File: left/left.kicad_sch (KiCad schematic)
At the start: 4 parts, among them J1 HDMI_C_1.4, SW1 SW_Push_Dual, U1 Raspberry_Pi_Pico

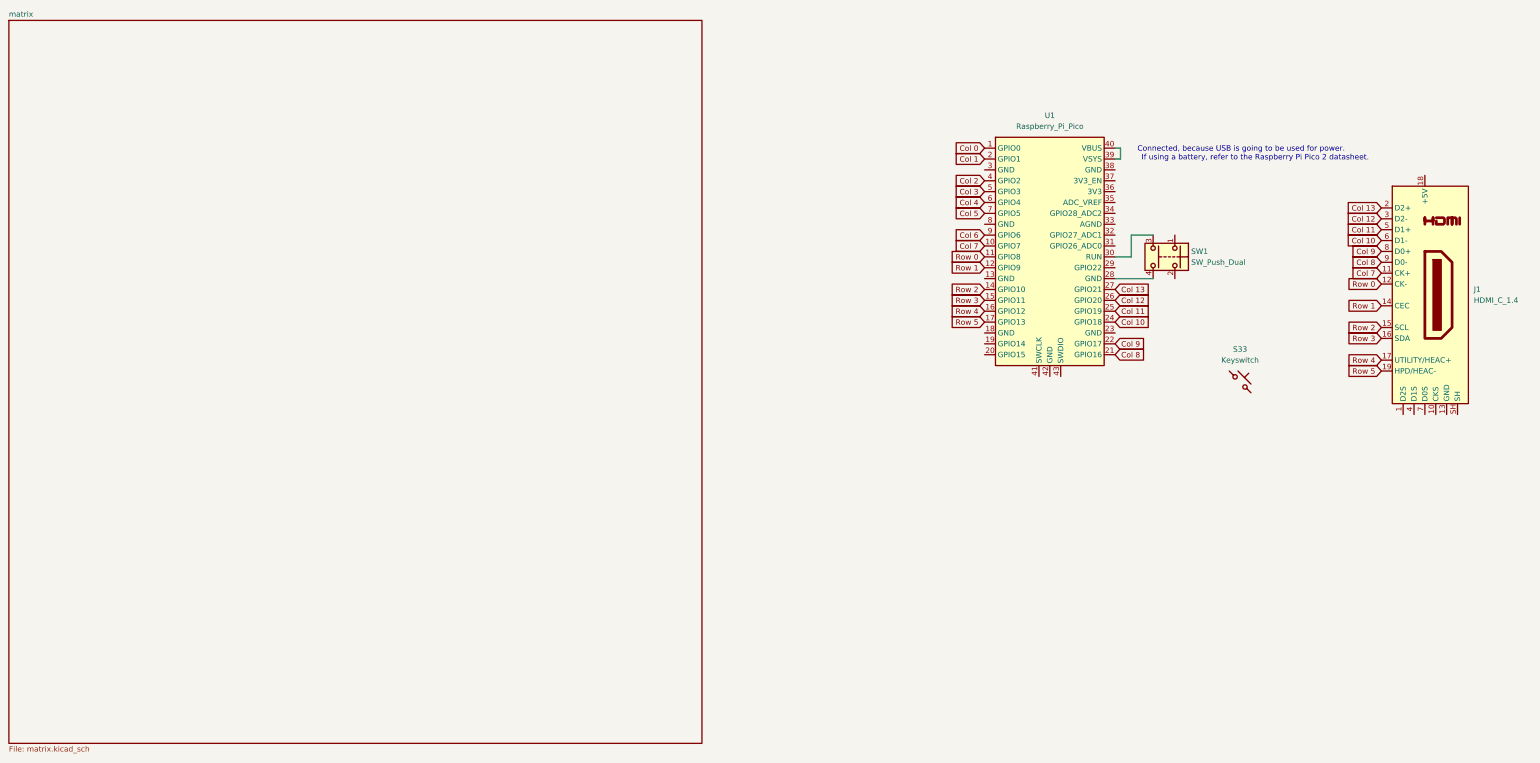
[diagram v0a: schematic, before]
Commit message: Fix issues from update to KiCad 9
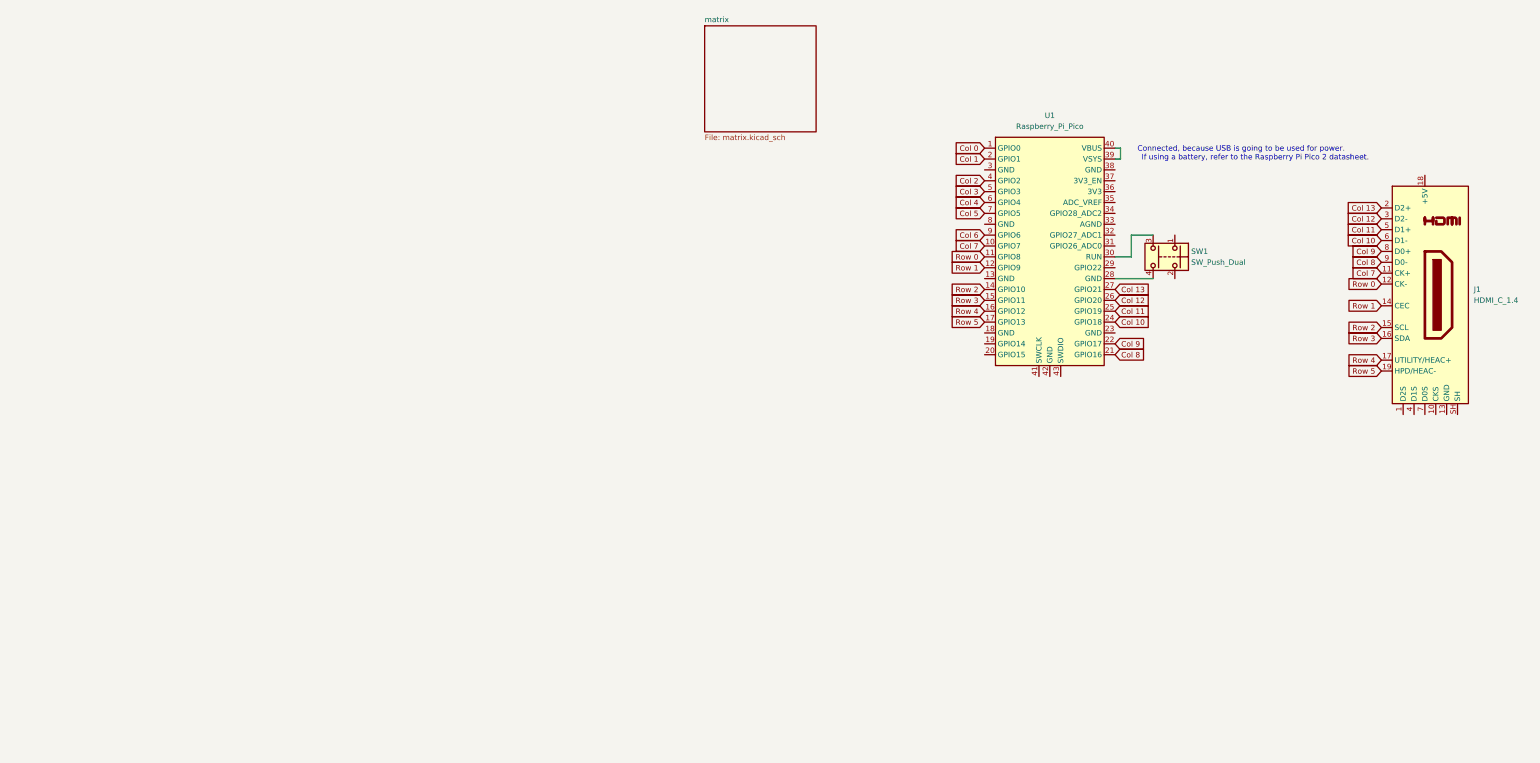
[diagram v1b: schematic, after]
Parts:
- removed S33: Keyswitch, ScottoKeebs_Hotswap:Hotswap_MX_1.00u, symbol ScottoKeebs:Placeholder_Keyswitch
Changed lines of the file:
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@@
 (kicad_sch
-	(version 20231120)
+	(version 20250114)
 	(generator "eeschema")
-	(generator_version "8.0")
+	(generator_version "9.0")
 	(paper "A4")
+	(text "If using a battery, refer to the Raspberry Pi Pico 2 datasheet.\n"
+		(exclude_from_sim no)
+		(at 96.266 31.496 0)
+		(effects
+			(font
+				(size 1.27 1.27)
+			)
+		)
+	)
+	(text "Connected, because USB is going to be used for power."
+		(exclude_from_sim no)
+		(at 92.964 29.464 0)
+		(effects
+			(font
+				(size 1.27 1.27)
+			)
+		)
+	)
 	(wire
 		(pts
@@
 		)
 	)
-	(text "If using a battery, refer to the Raspberry Pi Pico 2 datasheet.\n"
-		(exclude_from_sim no)
-		(at 96.266 31.496 0)
-		(effects
-			(font
-				(size 1.27 1.27)
-			)
-		)
-	)
-	(text "Connected, because USB is going to be used for power."
-		(exclude_from_sim no)
-		(at 92.964 29.464 0)
-		(effects
-			(font
-				(size 1.27 1.27)
-			)
-		)
-	)
 	(global_label "Row 2"
 		(shape input)
@@
 				(justify right)
 				(hide yes)
-			)
-		)
-	)
-	(symbol
-		(lib_id "ScottoKeebs:Placeholder_Keyswitch")
-		(at 92.71 83.82 0)
-		(unit 1)
-		(exclude_from_sim no)
-		(in_bom yes)
-		(on_board yes)
-		(dnp no)
-		(fields_autoplaced yes)
-		(property "Reference" "S33"
-			(at 92.71 76.2 0)
-			(effects
-				(font
-					(size 1.27 1.27)
-				)
-			)
-		)
-		(property "Value" "Keyswitch"
-			(at 92.71 78.74 0)
-			(effects
-				(font
-					(size 1.27 1.27)
-				)
-			)
-		)
-		(property "Footprint" "ScottoKeebs_Hotswap:Hotswap_MX_1.00u"
-			(at 92.71 83.82 0)
-			(effects
-				(font
-					(size 1.27 1.27)
-				)
-				(hide yes)
-			)
-		)
-		(property "Datasheet" "~"
-			(at 92.71 83.82 0)
-			(effects
-				(font
-					(size 1.27 1.27)
-				)
-				(hide yes)
-			)
-		)
-		(property "Description" "Push button switch, normally open, two pins, 45° tilted"
-			(at 92.71 83.82 0)
-			(effects
-				(font
-					(size 1.27 1.27)
-				)
-				(hide yes)
-			)
-		)
-		(pin "2"
-		)
-		(pin "1"
-		)
-		(instances
-			(project ""
-				(path "/6768e4e1-ee9a-4437-ba1f-295b12420b2f"
-					(reference "S33")
-					(unit 1)
-				)
 			)
 		)
@@
 	)
 	(sheet
-		(at -194.945 -0.635)
-		(size 161.925 168.91)
+		(at -32.385 0.635)
+		(size 26.035 24.765)
+		(exclude_from_sim no)
+		(in_bom yes)
+		(on_board yes)
+		(dnp no)
 		(fields_autoplaced yes)
 		(stroke
@@
 		)
 		(property "Sheetname" "matrix"
-			(at -194.945 -1.3466 0)
+			(at -32.385 -0.0766 0)
 			(effects
 				(font
@@
 		)
 		(property "Sheetfile" "matrix.kicad_sch"
-			(at -194.945 168.8596 0)
+			(at -32.385 25.9846 0)
 			(effects
 				(font
@@
 		)
 	)
+	(embedded_fonts no)
 )

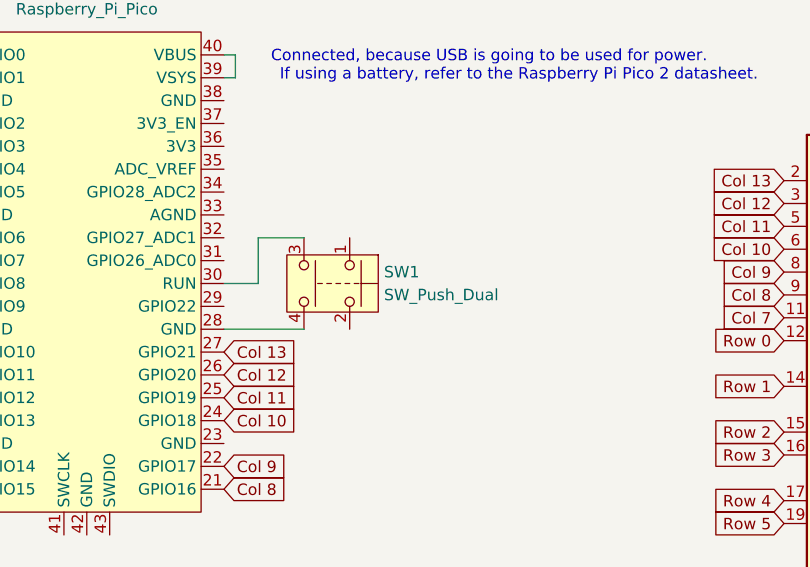
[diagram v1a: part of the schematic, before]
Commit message: Add OSHW logo
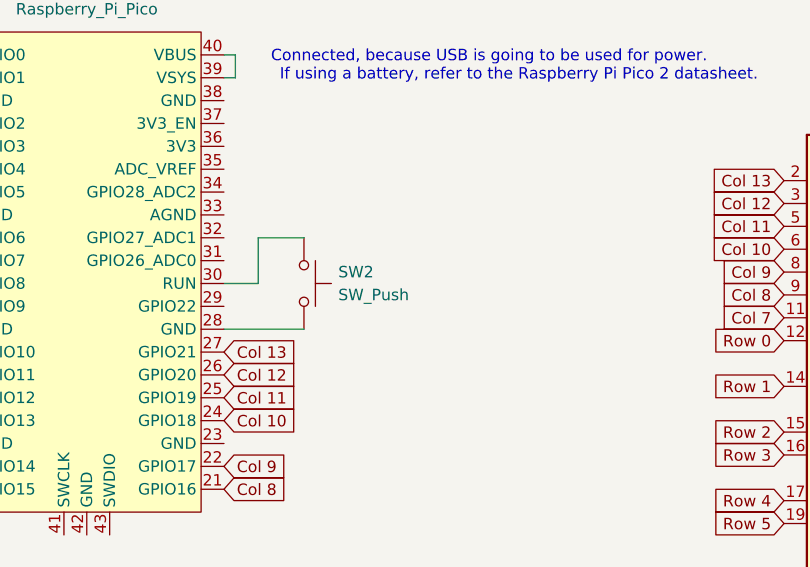
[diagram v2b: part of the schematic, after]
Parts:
- removed SW1: SW_Push_Dual, symbol Switch:SW_Push_Dual
- added SW2: SW_Push, Button_Switch_SMD:Panasonic_EVQPUJ_EVQPUA, symbol Switch:SW_Push
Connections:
- net at U1.30 (RUN): now also SW2.1
- net at U1.28 (GND): now also SW2.2
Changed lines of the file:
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@@
-	)
-	(symbol
-		(lib_id "Switch:SW_Push_Dual")
-		(at 74.93 54.61 270)
-		(unit 1)
-		(exclude_from_sim no)
-		(in_bom yes)
-		(on_board yes)
-		(dnp no)
-		(fields_autoplaced yes)
-		(property "Reference" "SW1"
-			(at 81.28 53.3399 90)
-			(effects
-				(font
-					(size 1.27 1.27)
-				)
-				(justify left)
-			)
-		)
-		(property "Value" "SW_Push_Dual"
-			(at 81.28 55.8799 90)
-			(effects
-				(font
-					(size 1.27 1.27)
-				)
-				(justify left)
-			)
-		)
-		(property "Footprint" ""
-			(at 82.55 54.61 0)
-			(effects
-				(font
-					(size 1.27 1.27)
-				)
-				(hide yes)
-			)
-		)
-		(property "Datasheet" "~"
-			(at 74.93 54.61 0)
-			(effects
-				(font
-					(size 1.27 1.27)
-				)
-				(hide yes)
-			)
-		)
-		(property "Description" "Push button switch, generic, symbol, four pins"
-			(at 74.93 54.61 0)
-			(effects
-				(font
-					(size 1.27 1.27)
-				)
-				(hide yes)
-			)
-		)
-		(pin "4"
-		)
-		(pin "3"
-		)
-		(pin "2"
-		)
-		(pin "1"
-		)
-		(instances
-			(project ""
-				(path "/6768e4e1-ee9a-4437-ba1f-295b12420b2f"
-					(reference "SW1")
-					(unit 1)
-				)
-			)
-		)
 	)
 	(symbol
@@
 					(unit 1)
 				)
+			)
+		)
+	)
+	(symbol
+		(lib_id "Switch:SW_Push")
+		(at 72.39 54.61 270)
+		(unit 1)
+		(exclude_from_sim no)
+		(in_bom yes)
+		(on_board yes)
+		(dnp no)
+		(fields_autoplaced yes)
+		(property "Reference" "SW2"
+			(at 76.2 53.3399 90)
+			(effects
+				(font
+					(size 1.27 1.27)
+				)
+				(justify left)
+			)
+		)
+		(property "Value" "SW_Push"
+			(at 76.2 55.8799 90)
+			(effects
+				(font
+					(size 1.27 1.27)
+				)
+				(justify left)
+			)
+		)
+		(property "Footprint" "Button_Switch_SMD:Panasonic_EVQPUJ_EVQPUA"
+			(at 77.47 54.61 0)
+			(effects
+				(font
+					(size 1.27 1.27)
+				)
+				(hide yes)
+			)
+		)
+		(property "Datasheet" "~"
+			(at 77.47 54.61 0)
+			(effects
+				(font
+					(size 1.27 1.27)
+				)
+				(hide yes)
+			)
+		)
+		(property "Description" "Push button switch, generic, two pins"
+			(at 72.39 54.61 0)
+			(effects
+				(font
+					(size 1.27 1.27)
+				)
+				(hide yes)
+			)
+		)
+		(pin "2"
+		)
+		(pin "1"
+		)
+		(instances
+			(project ""
+				(path "/6768e4e1-ee9a-4437-ba1f-295b12420b2f"
+					(reference "SW2")
+					(unit 1)
+				)
